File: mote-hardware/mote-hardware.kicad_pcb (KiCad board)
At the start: 2 copper layers, 93.6 x 102.8 mm, 67 parts, among them J1 USB_C_Receptacle_USB2.0_14P, J2 JST_XH2.54-SP, J4 SM03B-SRSS-TB, J5 Conn_01x03_Pin, J6 Conn_01x03_Pin, J7 JST_PH_B6B, J8 JST_PH_B6B, SW1 SW_Push, SW2 SW_Push, U1 RP2354_60QFN, U2 NCP1117-3.3_SOT223, U4 RP Radio Module 2, U5 DRV8833PW, U9 LSM6DS3, Y1 ABM8-272-T3

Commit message: mend
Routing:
- net Net-(U4-nIRQ): track 2.70 -> 1.72 mm
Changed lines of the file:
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@@
-	)
-	(segment
-		(start 101.43 126.098)
-		(end 101.43 127.084)
-		(width 0.15)
-		(layer "F.Cu")
-		(net 39)
 	)
 	(segment

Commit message: mend
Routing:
- net (no net): track 0.00 -> 17.4 mm, vias 0 -> 8
- net GND: track 76.2 -> 77.6 mm, vias 49 -> 50
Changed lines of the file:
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@@
 		(layer "Edge.Cuts")
+	)
+	(via
+		(at 107.188 120.396)
+		(size 0.6)
+		(drill 0.35)
+		(layers "F.Cu" "B.Cu")
+		(net 0)
+	)
+	(via
+		(at 106.172 99.822)
+		(size 0.6)
+		(drill 0.35)
+		(layers "F.Cu" "B.Cu")
+		(net 0)
+	)
+	(via
+		(at 92.456 114.808)
+		(size 0.6)
+		(drill 0.35)
+		(layers "F.Cu" "B.Cu")
+		(net 0)
+	)
+	(via
+		(at 108.458 99.06)
+		(size 0.6)
+		(drill 0.35)
+		(layers "F.Cu" "B.Cu")
+		(net 0)
+	)
+	(via
+		(at 110.49 97.028)
+		(size 0.6)
+		(drill 0.35)
+		(layers "F.Cu" "B.Cu")
+		(net 0)
+	)
+	(via
+		(at 111.252 120.396)
+		(size 0.6)
+		(drill 0.35)
+		(layers "F.Cu" "B.Cu")
+		(net 0)
+	)
+	(via
+		(at 92.456 117.856)
+		(size 0.6)
+		(drill 0.35)
+		(layers "F.Cu" "B.Cu")
+		(net 0)
+	)
+	(via
+		(at 102.362 120.396)
+		(size 0.6)
+		(drill 0.35)
+		(layers "F.Cu" "B.Cu")
+		(net 0)
+	)
+	(segment
+		(start 107.188 120.396)
+		(end 111.252 120.396)
+		(width 0.6)
+		(layer "B.Cu")
+		(net 0)
+	)
+	(segment
+		(start 106.172 99.822)
+		(end 107.696 99.822)
+		(width 0.6)
+		(layer "B.Cu")
+		(net 0)
+	)
+	(segment
+		(start 107.696 99.822)
+		(end 108.458 99.06)
+		(width 0.6)
+		(layer "B.Cu")
+		(net 0)
+	)
+	(segment
+		(start 108.458 99.06)
+		(end 110.49 97.028)
+		(width 0.6)
+		(layer "B.Cu")
+		(net 0)
+	)
+	(segment
+		(start 92.456 117.856)
+		(end 92.456 114.808)
+		(width 0.6)
+		(layer "B.Cu")
+		(net 0)
+	)
+	(segment
+		(start 102.362 120.396)
+		(end 107.188 120.396)
+		(width 0.6)
+		(layer "B.Cu")
+		(net 0)
 	)
 	(segment
@@
 	)
 	(segment
+		(start 98.298 112.776)
+		(end 97.536 112.014)
+		(width 0.15)
+		(layer "F.Cu")
+		(net 1)
+	)
+	(segment
 		(start 99.93 126.098)
 		(end 99.93 124.840462)
@@
 	)
 	(segment
+		(start 97.536 112.014)
+		(end 97.282 112.014)
+		(width 0.15)
+		(layer "F.Cu")
+		(net 1)
+	)
+	(segment
 		(start 106.68 127.398)
 		(end 108.094 127.398)
@@
 		(size 0.6)
 		(drill 0.35)
+		(layers "F.Cu" "B.Cu")
+		(net 1)
+	)
+	(via
+		(at 97.282 112.014)
+		(size 0.6)
+		(drill 0.35)

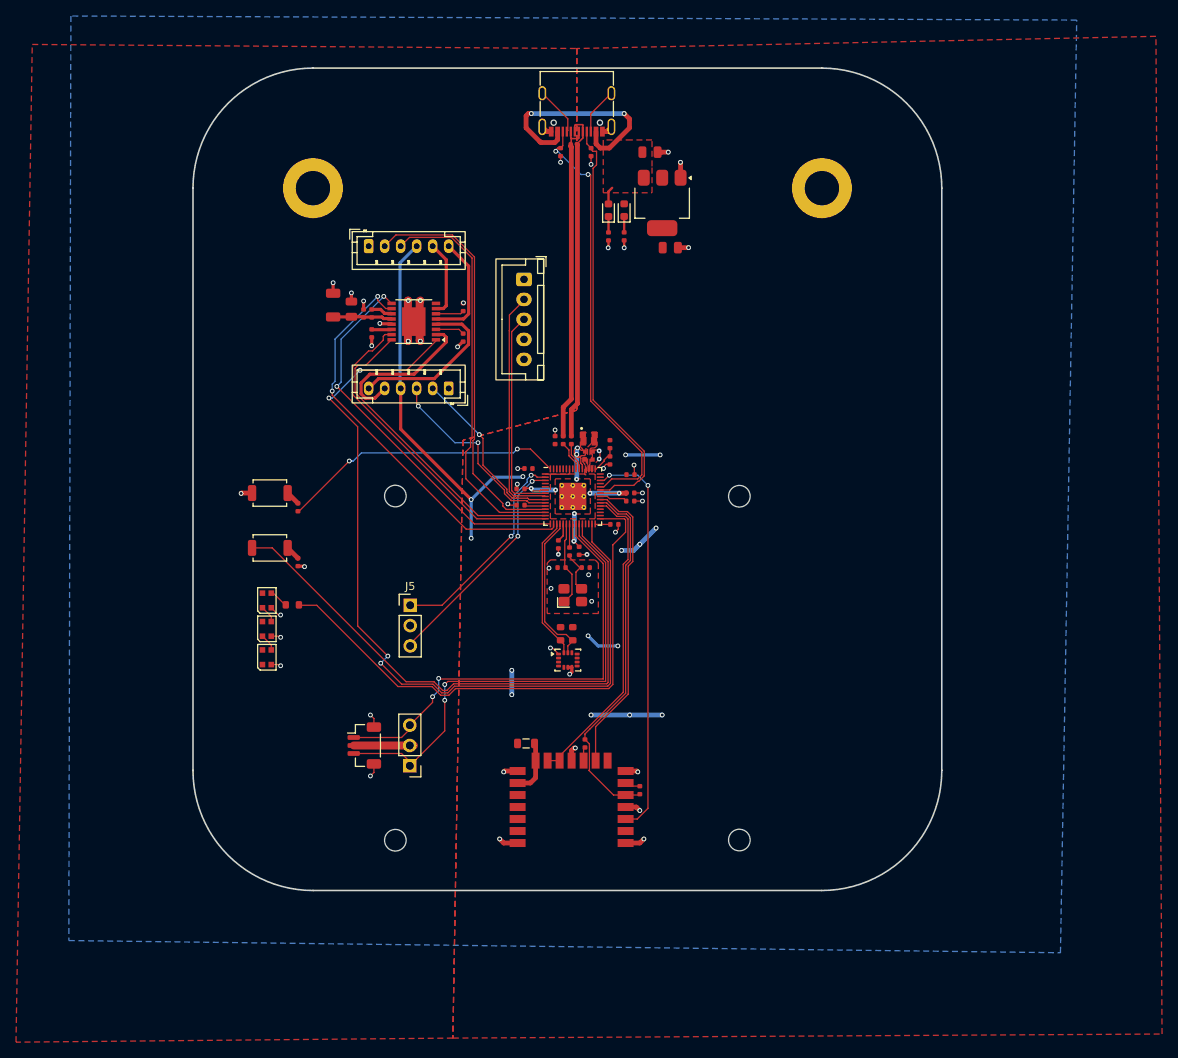
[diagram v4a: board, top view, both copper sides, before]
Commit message: Rearrange to make room for motors
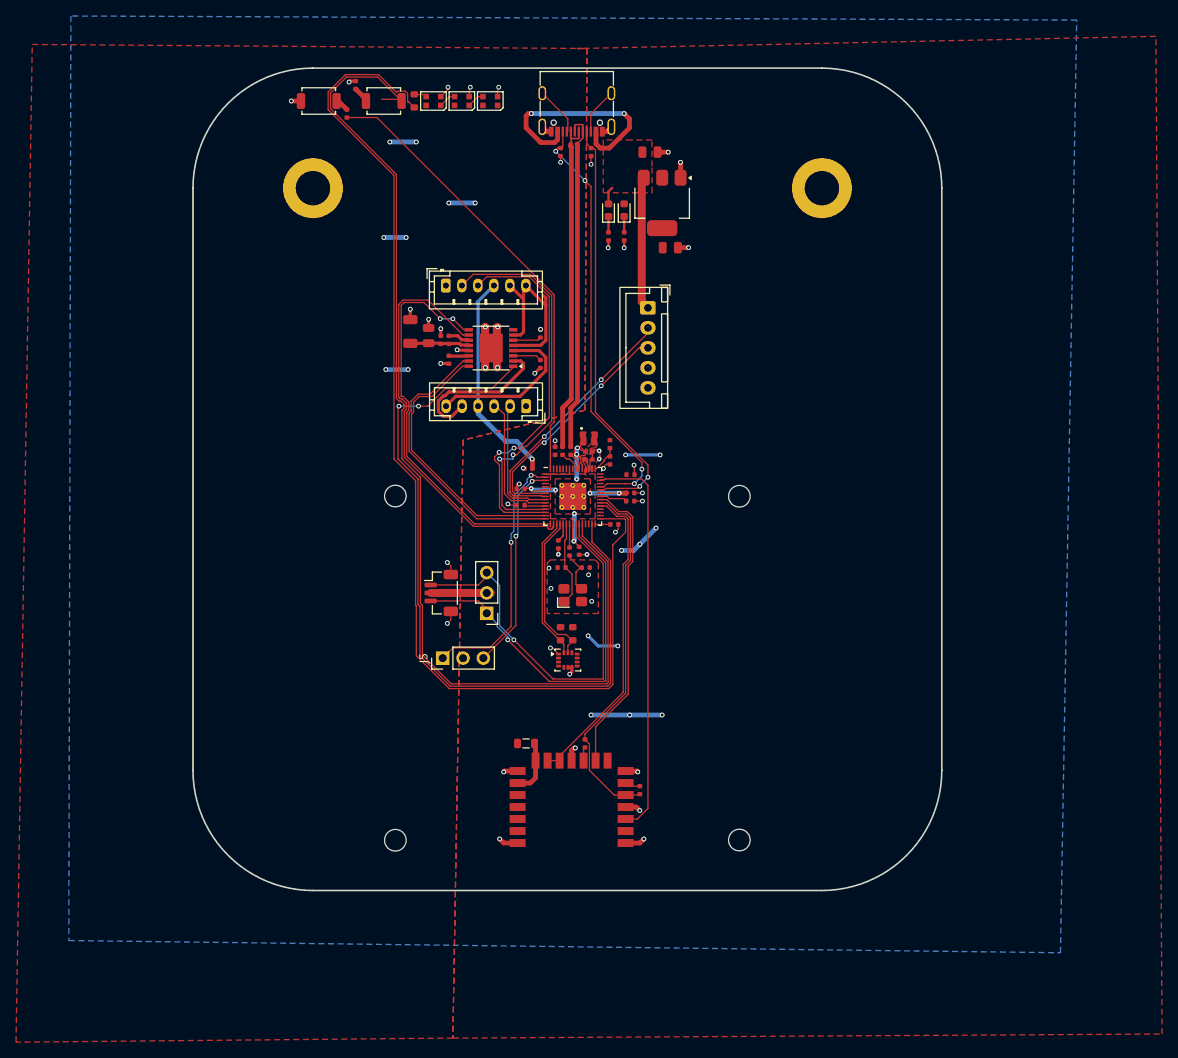
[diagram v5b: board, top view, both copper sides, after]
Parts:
- moved D5 74.9 mm to (89.8, 43.6), turned to 180 degrees
- moved D4 70.3 mm to (86.2, 43.6), turned to 180 degrees
- moved D3 65.8 mm to (82.7, 43.6), turned to 180 degrees
- moved R13 64.8 mm to (80.3, 43.6), turned to 90 degrees
- moved R4 60.1 mm to (72.9, 41.7), turned to 90 degrees
- moved SW2 57.6 mm to (76.5, 43.6), turned to 0 degrees
- moved R6 49.6 mm to (71.8, 45.2)
- moved SW1 49.4 mm to (68.3, 43.6)
- moved J4 21.4 mm to (83.6, 105.1)
- moved J6 21.4 mm to (89.3, 107.7)
- moved J2 15.9 mm to (109.5, 69.5)
- moved J8 10.8 mm to (84.2, 66.7)
- moved C19 10.2 mm to (84.6, 73.5)
- moved C21 10.2 mm to (82.1, 73.0)
- moved R11 10.2 mm to (96.0, 76.5)
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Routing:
- net /status_led_tx: track 68.8 -> 140.1 mm
- net /rp2354/RUN: track 73.4 -> 134.8 mm
- net /+5v: track 38.3 -> 67.2 mm, vias 2 -> 10
- net /rp2354/QSPI_SS: track 35.9 -> 57.0 mm, vias 2 -> 0
- net (no net): track 17.4 -> 0.00 mm, vias 8 -> 0
- net /rp2354/SWD: track 61.5 -> 48.1 mm, vias 2 -> 1
- net /motor_standby: track 104.8 -> 95.3 mm, vias 4 -> 2
- net /motor_left_encoder_b: track 25.0 -> 17.2 mm, vias 2 -> 0
- net /+3v3: track 71.1 -> 64.3 mm, vias 7 -> 11
- net /motor_left_encoder_a: track 22.0 -> 16.1 mm, vias 1 -> 0
- net /rp2354/UART0_TX: track 26.7 -> 32.0 mm
- net /rp2354/SWCLK: track 56.9 -> 52.0 mm, vias 2 -> 1
- net /motor_left_input_b: track 40.8 -> 36.1 mm
- net /motor_left_input_a: track 39.2 -> 35.0 mm
- net /lidar_tx: track 26.4 -> 30.0 mm, vias 0 -> 2
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
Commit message: Update board cutout for back connectors
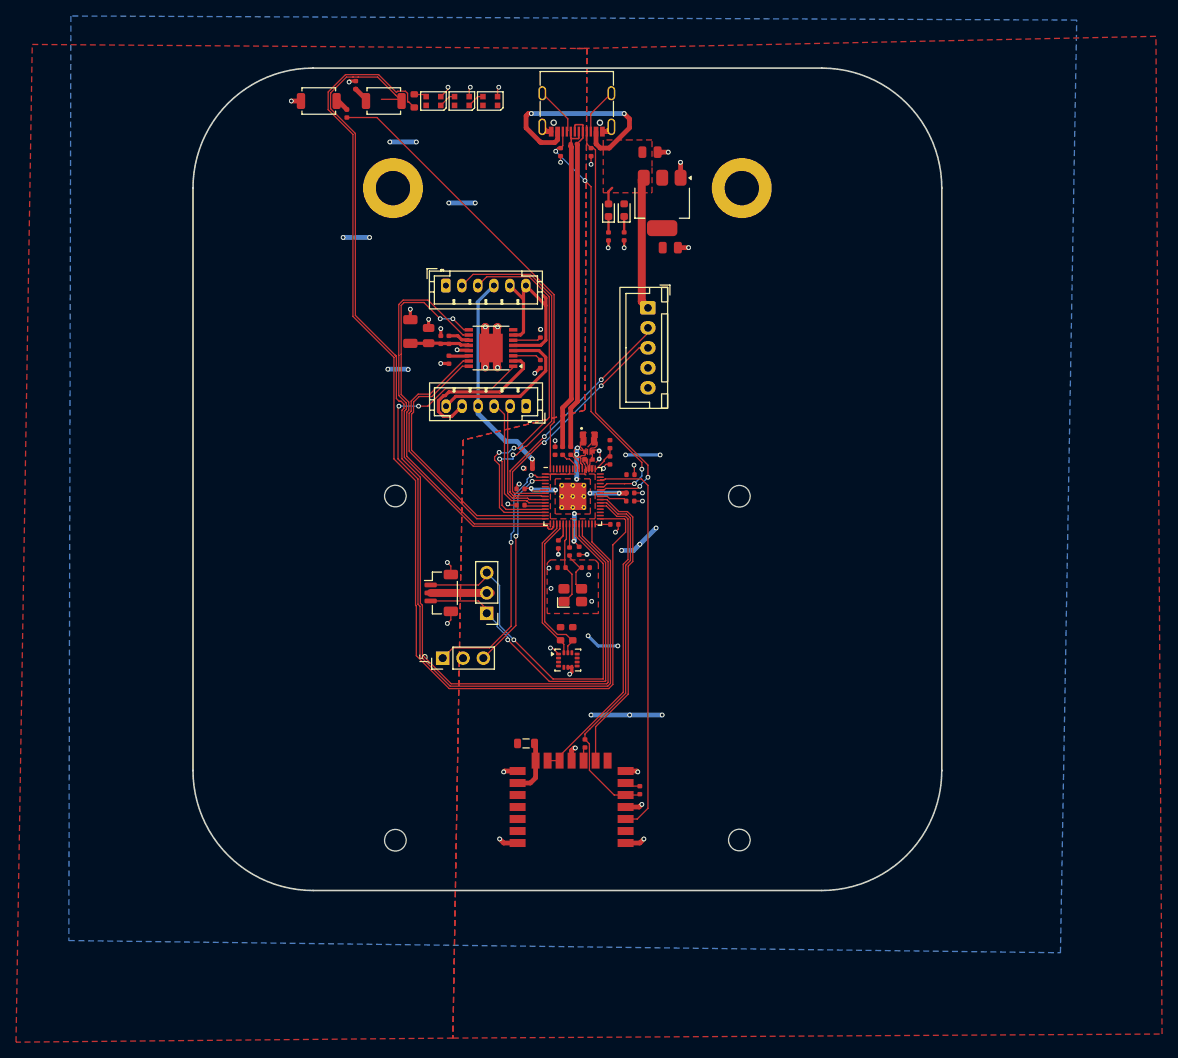
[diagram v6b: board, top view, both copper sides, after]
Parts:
- moved H5 10.0 mm to (121.2, 54.5)
- moved H6 10.0 mm to (77.6, 54.5)

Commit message: Pass DRC
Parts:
- moved C12 0.15 mm to (97.7, 87.4)
- moved R8 0.08 mm to (99.7, 87.4)
- moved R7 0.08 mm to (98.7, 87.4)
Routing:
- net /+3v3: track 64.3 -> 67.2 mm
- net /rp2354/RUN: track 135.0 -> 132.2 mm
- net Net-(J8-Pin_5): track 9.43 -> 7.81 mm
- net Net-(J8-Pin_6): track 13.5 -> 12.1 mm
- net GND: track 77.2 -> 78.1 mm
